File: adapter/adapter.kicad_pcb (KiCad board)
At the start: 2 copper layers, 93.5 x 50.9 mm, 64 parts, among them J1 Serial, J10 Ribbon, J11 Ribbon, J12 Ribbon, J13 serial, J14 serial, J2 Serial, J3 battery charge, J4 RGB, J5 RGB, J6 battery charge, J7 trackball, J8 trackball, J9 Ribbon, SW1 SW_SPST, SW2 SW_SPST, SW3 SW_SPDT, SW4 SW_SPDT, U1 eliteC, U2 eliteC

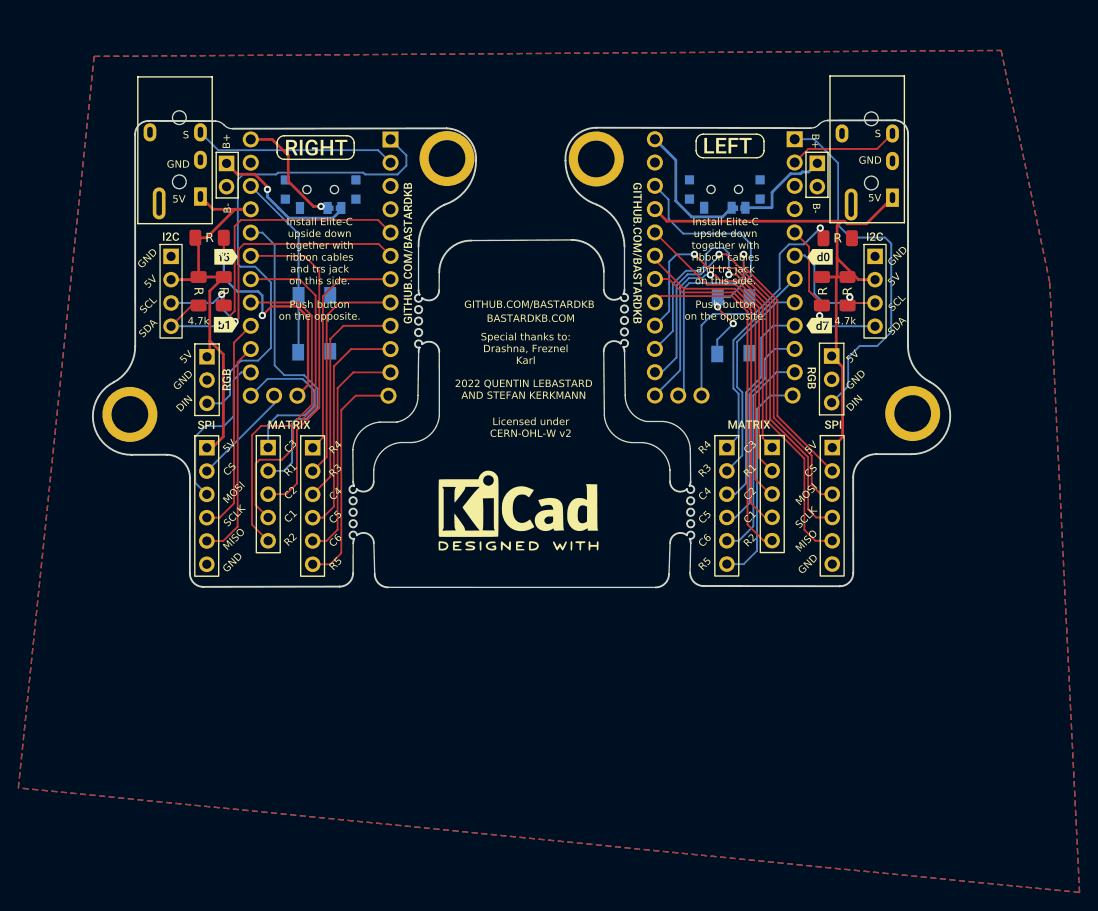
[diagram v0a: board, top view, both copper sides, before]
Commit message: updated design
- swapped high frequency pins from matrix to spi
- removed jacks and serial resistors
- added ph2 battery headers
- moved reset buttons
- gerbers added to production dir
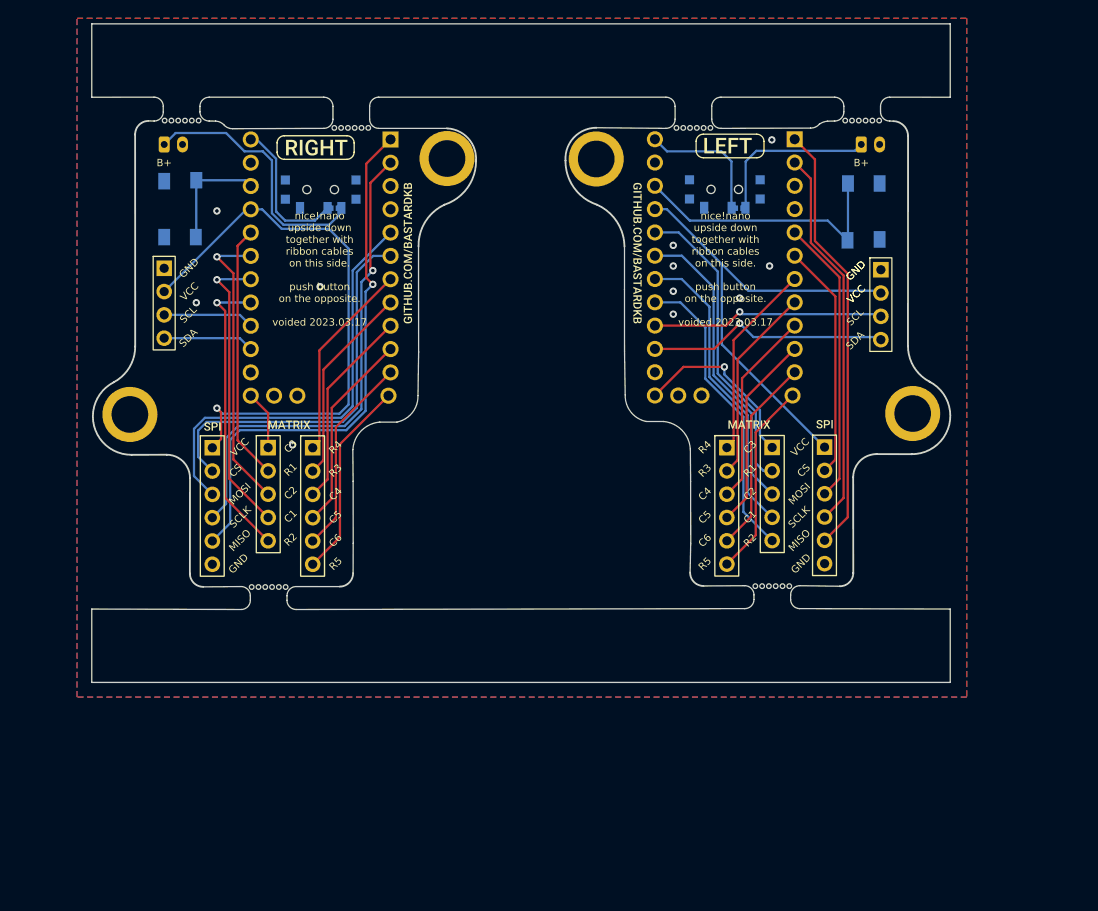
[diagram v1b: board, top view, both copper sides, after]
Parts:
- removed G*** (x2): LOGO, LOGO
- removed J1, J2: Serial, Library:Jack_3.5mm_PJ320E_Horizontal
- removed the J13 at (194.0, 82.0)
- removed J14: serial, Library:PinHeader_1x04_P2.54mm_Vertical
- removed J3, J6: battery charge, Library:PinHeader_1x02_P2.54mm_Vertical
- removed J4, J5: RGB, Library:header1x03
- removed R1, R3, R5, R6: 5.1k, Library:R_1206_handsolder
- removed R2, R4: 4.7k, Library:R_1206_handsolder
- removed kibuzzard-61F019CB (x4): G***, kibuzzard-61F019CB
- removed kibuzzard-61F01C84 (x2): G***, kibuzzard-61F01C84
- removed kibuzzard-6208EDFE: G***, kibuzzard-6208EDFE
- removed kibuzzard-6208EE22: G***, kibuzzard-6208EE22
- removed kibuzzard-62093EDE: G***, kibuzzard-62093EDE
- removed kibuzzard-62094D1C: G***, kibuzzard-62094D1C
- removed kibuzzard-620B8D91 (x4): G***, kibuzzard-620B8D91
- added J13: serial, Library:PinHeader_1x04_P2.54mm_Vertical, F.Cu at (194.6, 83.4)
- added J13: serial, Library:PinHeader_1x04_P2.54mm_Vertical, F.Cu at (116.5, 83.2)
- added REF**: mousebites 2mm, marbastlib-various:mousebites_2.5mm, F.Cu at (127.9, 118.0)
- added REF**: JST_PH_B2B-PH-K_1x02_P2.00mm_Vertical, Connector_JST:JST_PH_B2B-PH-K_1x02_P2.00mm_Vertical, F.Cu at (192.5, 69.8)
- added REF**: mousebites 2mm, marbastlib-various:mousebites_2.5mm, F.Cu at (118.4, 67.2)
- added REF**: mousebites 2mm, marbastlib-various:mousebites_2.5mm, F.Cu at (174.2, 68.0)
- added REF**: mousebites 2mm, marbastlib-various:mousebites_2.5mm, F.Cu at (192.6, 67.2)
- added REF**: mousebites 2mm, marbastlib-various:mousebites_2.5mm, F.Cu at (136.9, 68.0)
- added REF**: mousebites 2mm, marbastlib-various:mousebites_2.5mm, F.Cu at (182.8, 117.9)
- added REF**: JST_PH_B2B-PH-K_1x02_P2.00mm_Vertical, Connector_JST:JST_PH_B2B-PH-K_1x02_P2.00mm_Vertical, F.Cu at (116.5, 69.8)
- moved SW1 19.3 mm to (118.2, 76.8), turned to 90 degrees
- moved SW2 18.9 mm to (192.8, 77.1)
- moved kibuzzard-61F01957 0.94 mm to (188.5, 100.2)
- moved kibuzzard-61F01957 0.92 mm to (188.5, 100.2)
- moved J8 0.84 mm to (188.5, 102.8)
- moved kibuzzard-61F01957 0.70 mm to (121.8, 100.5)
- moved kibuzzard-61F01957 0.63 mm to (121.8, 100.5)
- moved J7 0.60 mm to (121.8, 102.8)
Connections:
- U1 pad 1: rgb_r -> miso_l
- U1 pad 14: mosi_l -> (no net)
- U1 pad 15: miso_l -> sda_l
- U1 pad 16: sc_l -> scl_l
- U1 pad 2: serial_l -> sc_l
- U1 pad 28: split_hand_l -> (no net)
- U1 pad 29: ss_l -> (no net)
- U1 pad 5: sda_l -> mosi_l
- U1 pad 6: scl_l -> ss_l
- U2 pad 1: rgb_l -> miso_r
- U2 pad 14: mosi_r -> (no net)
- U2 pad 15: miso_r -> sda_r
- U2 pad 16: sc_r -> scl_r
- U2 pad 2: serial_r -> sc_r
- U2 pad 28: split_hand_r -> (no net)
- U2 pad 29: ss_r -> (no net)
- U2 pad 5: sda_r -> mosi_r
- U2 pad 6: scl_r -> ss_r
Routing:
- net rgb_r: track 54.5 -> 0.00 mm
- net rgb_l: track 40.4 -> 0.00 mm
- net miso_l: track 24.0 -> 59.2 mm, vias 0 -> 1
- net ss_l: track 11.3 -> 42.6 mm
- net sc_l: track 23.7 -> 53.8 mm, vias 0 -> 1
- net mosi_l: track 18.1 -> 46.9 mm
- net sda_l: track 38.7 -> 9.93 mm, vias 1 -> 0
- net split_hand_r: track 28.5 -> 0.00 mm, vias 1 -> 0
- net split_hand_l: track 26.5 -> 0.00 mm, vias 2 -> 0
- net scl_l: track 36.2 -> 9.93 mm, vias 2 -> 0
- net ss_r: track 49.0 -> 25.7 mm, vias 1 -> 0
- net serial_l: track 22.1 -> 0.00 mm
- net col3_r: track 39.8 -> 19.8 mm
- net mosi_r: track 49.5 -> 31.2 mm, vias 1 -> 0
- net bat_sw_l: track 16.2 -> 28.4 mm, vias 1 -> 0
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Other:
- board size 93.5 x 50.9 mm -> 93.6 x 71.8 mm
- board text added: "VCC"
- board text added: "n!n HOLDER 0.1"
- board text added: "nice!nano upside down together with ribbon cables on this side. push button on the opposite. voided 2023.03.17"
- board text removed: "2022 QUENTIN LEBASTARD AND STEFAN KERKMANN"
- board text removed: "4.7k"
- board text removed: "5V"
- board text removed: "B-"
- board text removed: "BASTARDKB.COM"
- board text removed: "DIN"
- board text removed: "ELITE-C HOLDER 2.1"
- board text removed: "GITHUB.COM/BASTARDKB"
- board text removed: "Install Elite-C upside down together with ribbon cables and trs jack on this side. Push button on the opposite."
- board text removed: "Licensed under CERN-OHL-W v2"
- board text removed: "S"
- board text removed: "Special thanks to: Drashna, Freznel Karl"
